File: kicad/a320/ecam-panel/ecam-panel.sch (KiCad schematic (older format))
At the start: 40 parts

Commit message: Adda RC circuit for CLR push buttons to debounce
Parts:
- removed R?: 10k, symbol R
- removed SW? (x2): SW_PUSH_SMALL_H, symbol SW_PUSH_SMALL_H
- added C3: 1uF, symbol C_Small
- added C5, C6, C7: 100nF, symbol C_Small
- added R1: 10k, symbol R
- added R2: 220, symbol R
- added SW17, SW18: SW_PUSH_SMALL_H, symbol SW_PUSH_SMALL_H
- gave numbers to parts that had none: 37
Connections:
- net labels added: GND, VCC
- net labels removed: +5V, CLK, GNDREF
- wire segments 112 -> 125
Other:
- moved on the sheet: C4, P1, R3, U3

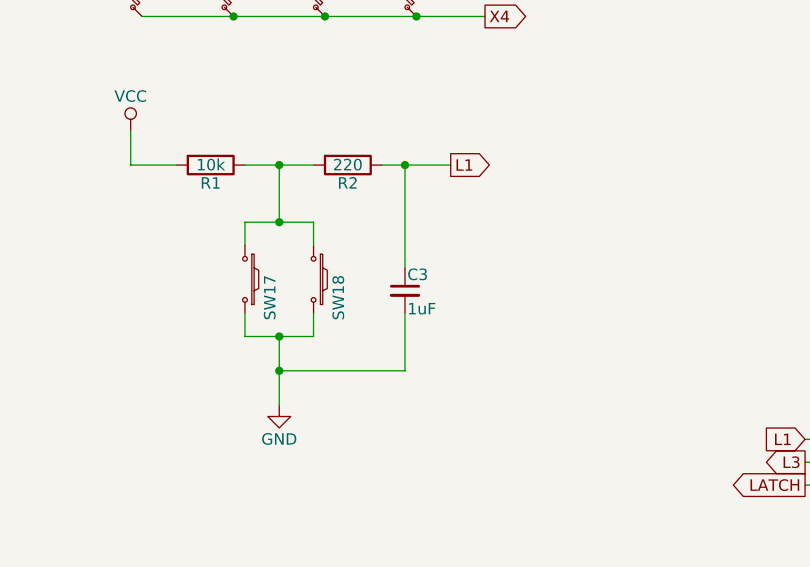
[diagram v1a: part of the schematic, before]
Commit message: Use a polarized capacitor for CLR button of ECAM panel
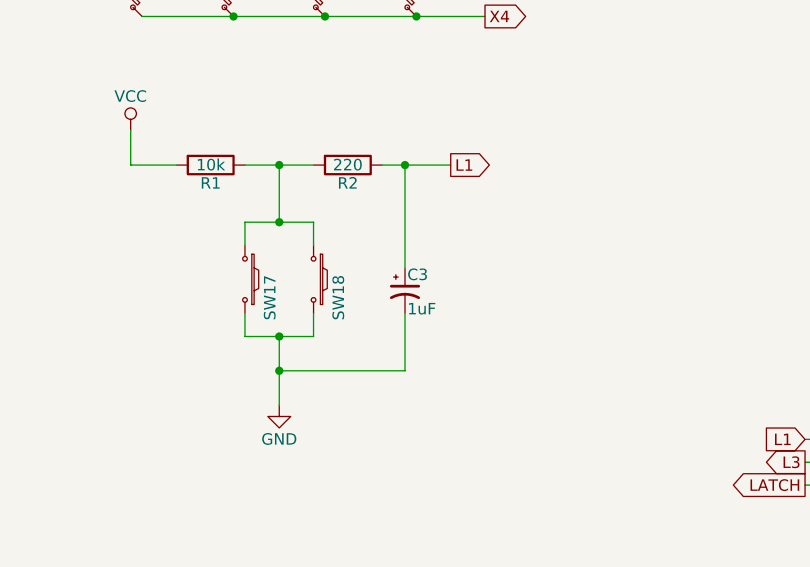
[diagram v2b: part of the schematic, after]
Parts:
- removed C3: 1uF, symbol C_Small
- added C3: 1uF, symbol CP1_Small
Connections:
- net GND: now also C3.2
- net L1: now also C3.1
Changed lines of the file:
@@
 	2850 4400 2850 4100
 Connection ~ 2850 4100
-$Comp
-L C_Small C3
-U 1 1 595354EB
-P 3400 3900
-F 0 "C3" H 3410 3970 50  0000 L CNN
-F 1 "1uF" H 3410 3820 50  0000 L CNN
-F 2 "" H 3400 3900 50  0000 C CNN
-F 3 "" H 3400 3900 50  0000 C CNN
-	1    3400 3900
-	1    0    0    -1
-$EndComp
 Wire Wire Line
 	2700 3700 2700 3600
@@
 	1    0    0    -1
 $EndComp
+$Comp
+L CP1_Small C3
+U 1 1 595770B6
+P 3400 3900
+F 0 "C3" H 3410 3970 50  0000 L CNN
+F 1 "1uF" H 3410 3820 50  0000 L CNN
+F 2 "" H 3400 3900 50  0000 C CNN
+F 3 "" H 3400 3900 50  0000 C CNN
+	1    3400 3900
+	1    0    0    -1
+$EndComp

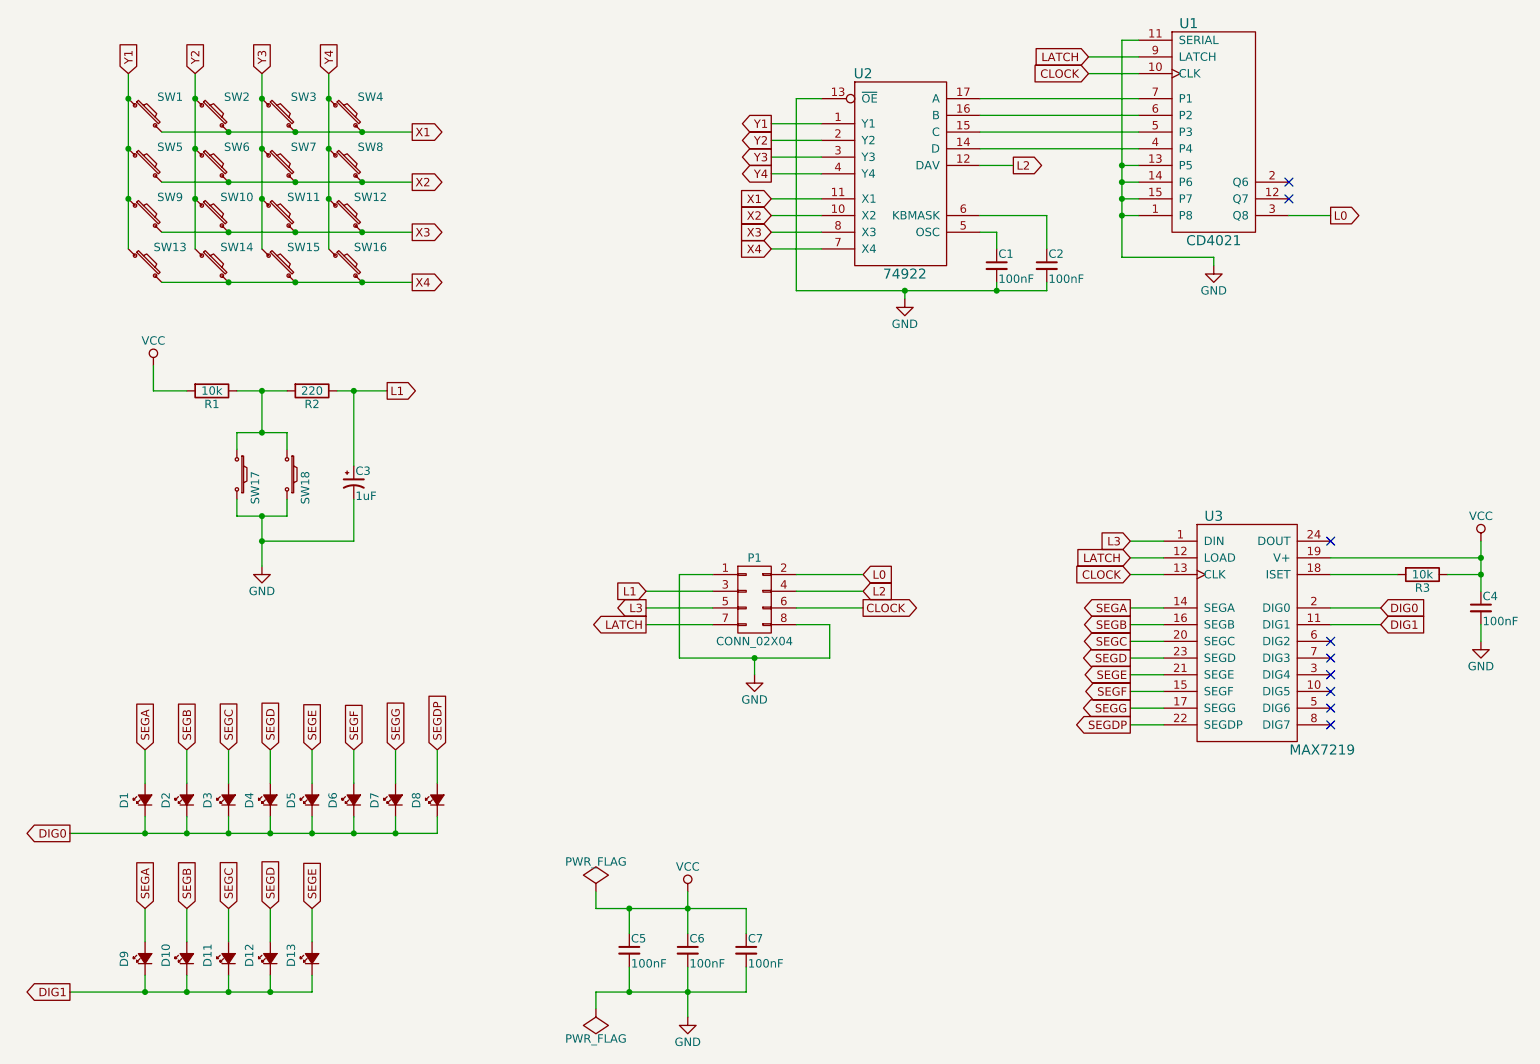
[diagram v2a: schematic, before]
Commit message: Use polarized cap for MM74C922's debounce in ECAM panel
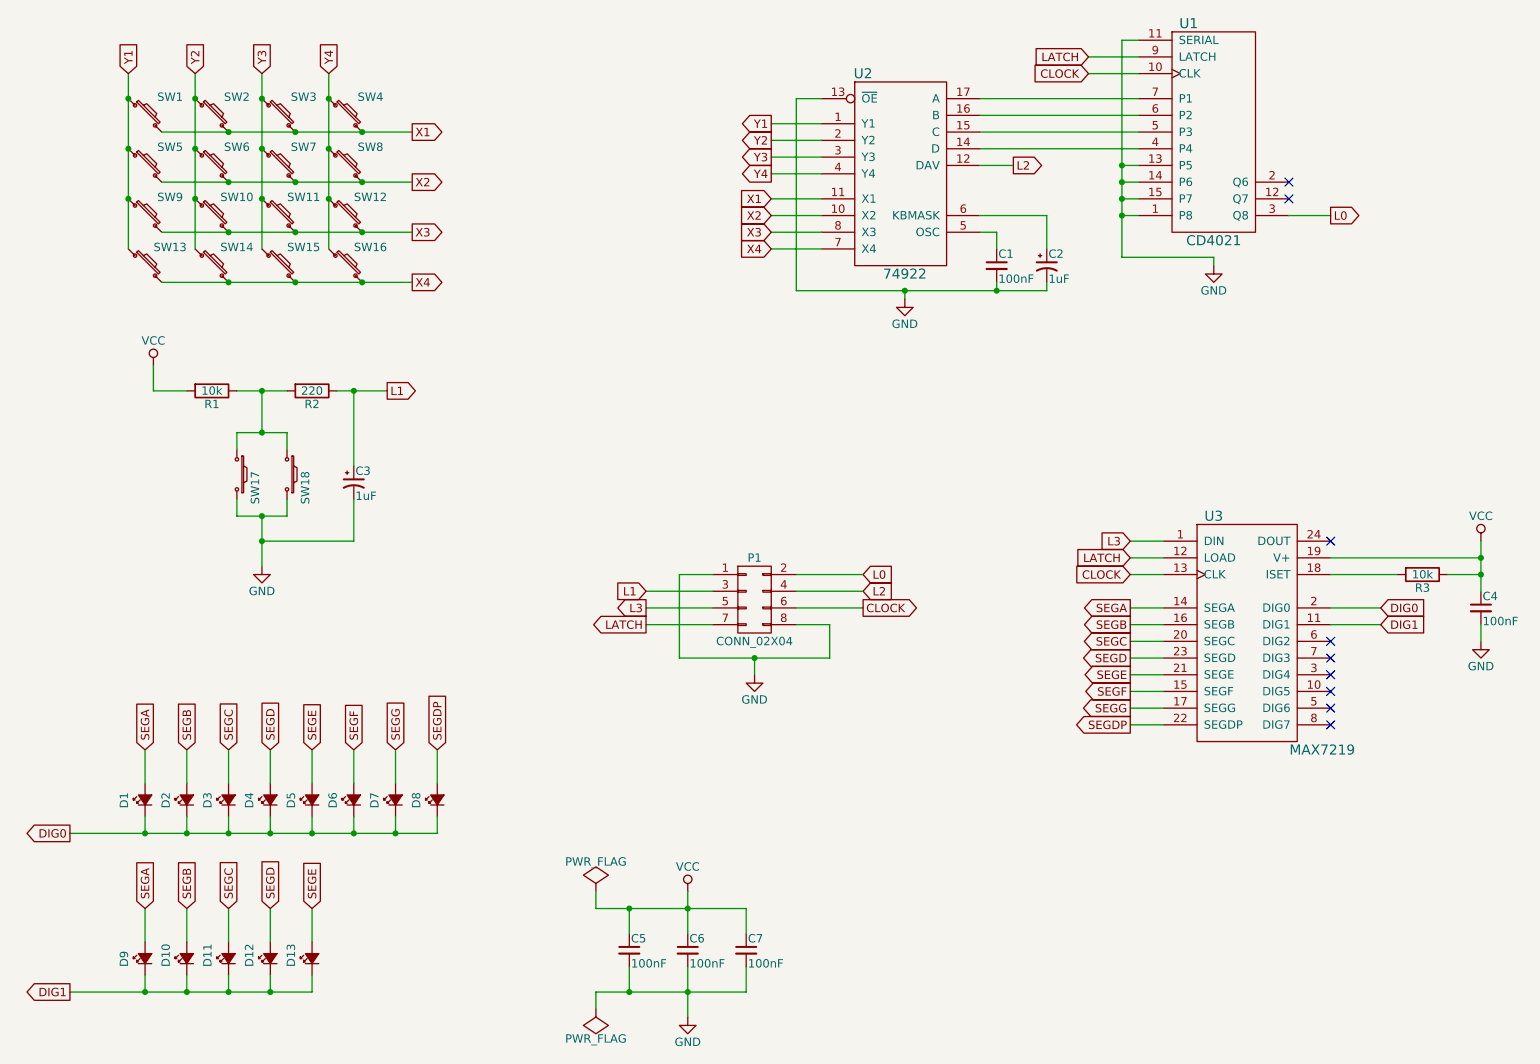
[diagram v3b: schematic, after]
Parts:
- removed C2: 100nF, symbol C_Small
- added C2: 1uF, symbol CP1_Small
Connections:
- net GND: now also C2.2
- net at U2.6 (KBMASK): now also C2.1
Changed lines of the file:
@@
-	1    0    0    -1
-$EndComp
-$Comp
-L C_Small C2
-U 1 1 5951E848
-P 7550 2600
-F 0 "C2" H 7560 2670 50  0000 L CNN
-F 1 "100nF" H 7560 2520 50  0000 L CNN
-F 2 "" H 7550 2600 50  0000 C CNN
-F 3 "" H 7550 2600 50  0000 C CNN
-	1    7550 2600
 	1    0    0    -1
 $EndComp
@@
 	8250 4350 8050 4350
 Wire Wire Line
-	3900 5900 3900 6000
-Wire Wire Line
-	3900 6000 1700 6000
+	3900 6000 3900 5900
+Wire Wire Line
+	1700 6000 3900 6000
 Wire Wire Line
 	3650 5900 3650 6000
@@
 DIG1
 Wire Wire Line
-	3150 6850 3150 6950
-Wire Wire Line
-	3150 6950 1700 6950
+	3150 6950 3150 6850
+Wire Wire Line
+	1700 6950 3150 6950
 Wire Wire Line
 	2900 6850 2900 6950
@@
 	3000 4100 3000 4000
 Wire Wire Line
-	2850 4400 2850 4100
+	2850 4100 2850 4400
 Connection ~ 2850 4100
 Wire Wire Line
@@
 	1    0    0    -1
 $EndComp
+$Comp
+L CP1_Small C2
+U 1 1 5958C1F6
+P 7550 2600
+F 0 "C2" H 7560 2670 50  0000 L CNN
+F 1 "1uF" H 7560 2520 50  0000 L CNN
+F 2 "" H 7550 2600 50  0000 C CNN
+F 3 "" H 7550 2600 50  0000 C CNN
+	1    7550 2600
+	1    0    0    -1
+$EndComp
